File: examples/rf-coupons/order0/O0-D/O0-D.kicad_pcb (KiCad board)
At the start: 4 copper layers, 60.5 x 67.1 mm, 25 parts, among them X17 Anchor, X20 Anchor, X23 Anchor

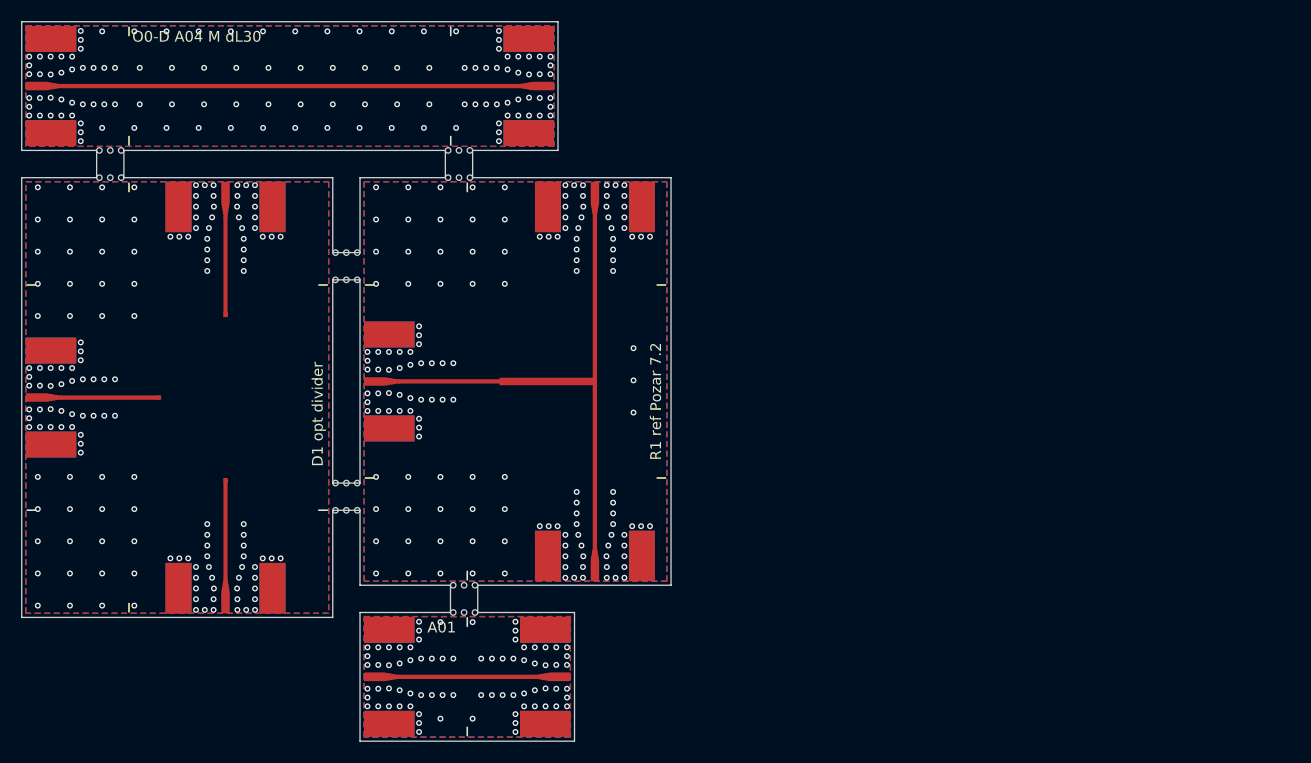
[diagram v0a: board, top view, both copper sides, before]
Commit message: Order 0: the uploads and predictions regenerated after the review
examples/rf-coupons/order0: generated from 73fe6527 (the tag carries it); KiCad
DRC under OSH Park's 4-layer rules 0 violations / 0 unconnected on all three.
`yapnr fab check` (oshpark-4l, oshpark-4l-fr408hr): O0-M 0 errors; O0-W and
O0-D stop on FAB-PLACEHOLDER until D2 and D1 are in (by design); warnings as
before (NPTH in the merged drill file; 1.511 mm of published layers):

- O0-M 120.1 x 144.3 mm, 26.9 sq in, 33 SMAs per copy, 32 tabs;
- O0-W 57.5 x 131.2 mm, 11.7 sq in, 16 SMAs, 15 tabs;
- O0-D 90.6 x 51.5 mm, 7.2 sq in, 12 SMAs, 9 tabs (A20 added).

Every stick has two or more tabs, all on edges without a launch; no plane via
under a silkscreen glyph; no mask web under 0.1 mm; the QR decodes from the
silkscreen render.

Predictions: the coupons on FR408HR and EM528 with the review's roughness
prior, the junction-corrected ring and stub (A12 notch 5.500 GHz FR408HR,
5.388 GHz EM528; A11 1.924 / 5.793 GHz), scalars.json and lines.csv. Boards A
and B regenerated (mask-opening anchors only; DRC unchanged).

docs/rf/order0: sizes and costs, R1/R1t as drawn, the renormalization to the
solver's port impedance (review H3), the C-pad method (M3), the loss basis
(M4), the scalars (L1), the sha256 rule (F9), the connector-fit pre-check, the
mask web note (L2), and the D1/D2 pages with the board around each window.

Co-Authored-By: Claude Opus 5.5 <noreply@anthropic.com>
Claude-Session: https://claude.ai/code/session_01NY8rMuBH8hTFjkoZyuqNZ7
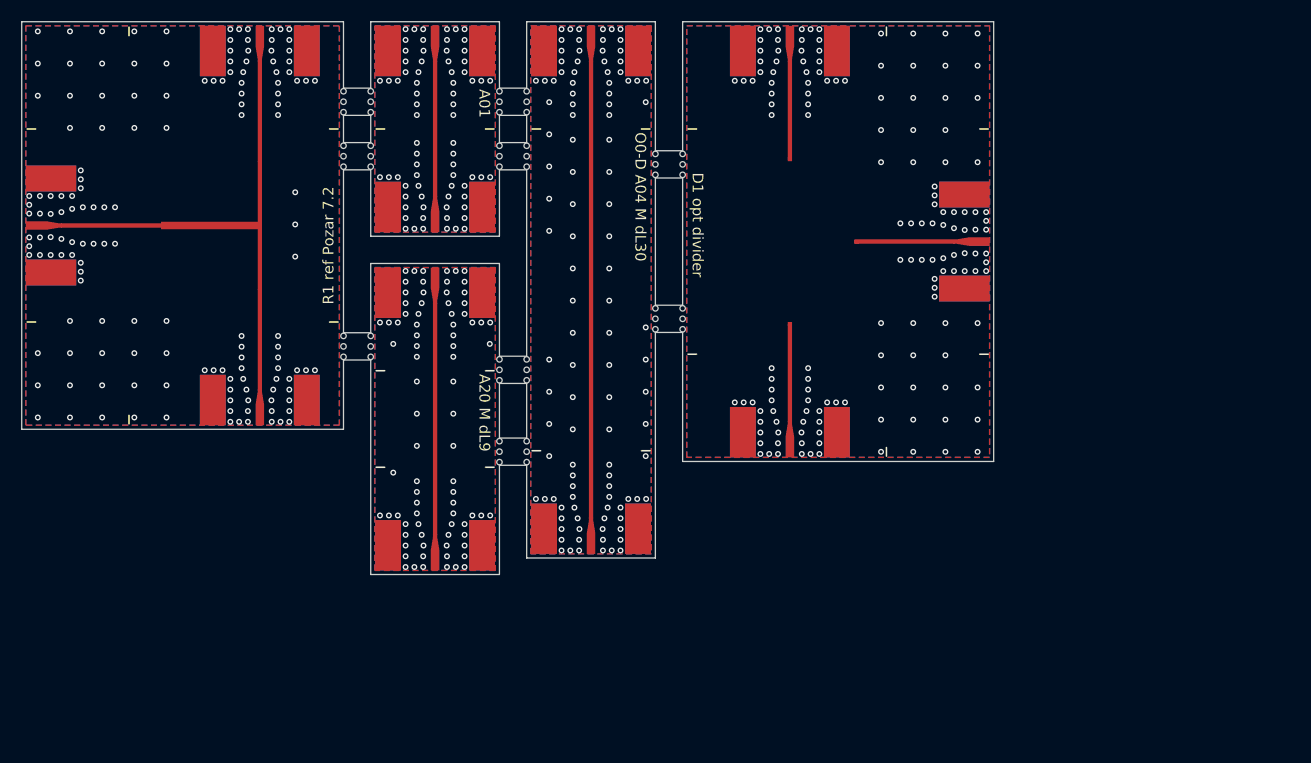
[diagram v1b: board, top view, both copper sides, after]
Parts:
- added JA20E: SMA_EdgeLaunch_Cinch_142-0701-851, SMA_EdgeLaunch_Cinch_142-0701-851, F.Cu at (58.5, 71.5)
- added JA20W: SMA_EdgeLaunch_Cinch_142-0701-851, SMA_EdgeLaunch_Cinch_142-0701-851, F.Cu at (58.5, 42.5)
- added MO_A20: MaskOpening, MaskOpening, F.Cu at (57.3, 45.0)
- added PHD1: Placeholder_D1, Placeholder_D1, F.Cu at (91.6, 40.5)
- moved JD1_1 91.8 mm to (110.6, 40.5), turned to 180 degrees
- moved JD1_3 76.5 mm to (91.6, 20.0), turned to -90 degrees
- moved MO_D1_1 75.0 mm to (97.6, 39.3)
- moved MO_D1_3 70.9 mm to (90.4, 22.5)
- moved X20 66.6 mm to (97.8, 40.5), turned to 180 degrees
- moved JA01W 61.5 mm to (58.5, 20.0), turned to -90 degrees
- moved X26 60.5 mm to (91.6, 32.8), turned to -90 degrees
- moved JD1_2 58.9 mm to (91.6, 61.0), turned to 90 degrees
- moved MO_A01 58.7 mm to (57.3, 22.5)
- moved JA04W 53.4 mm to (73.1, 20.0), turned to -90 degrees
- moved X23 52.6 mm to (91.6, 48.2), turned to 90 degrees
- moved MO_D1_2 52.2 mm to (90.4, 48.0)
- moved MO_D1_W 51.1 mm to (84.6, 32.0)
- moved JA04E 44.1 mm to (73.1, 70.0), turned to 90 degrees
- moved JA01E 43.1 mm to (58.5, 40.0), turned to 90 degrees
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- renumbered X17 to X20, X20 to X23, X23 to X26
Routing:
- net RF_A20: track 0.00 -> 21.6 mm
- net GND_R1: vias 151 -> 149
- net GND_D1: vias 148 -> 146
- net GND_A20: vias 0 -> 81
- net GND_A04: vias 116 -> 107
- net GND_A01: vias 76 -> 72
- added copper zone on B.Cu, net GND_A20
- added copper zone on F.Cu, net GND_A20
- added copper zone on In1.Cu, net GND_A20
- added copper zone on In2.Cu, net GND_A20
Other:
- board size 60.5 x 67.1 mm -> 90.6 x 51.5 mm
- board text added: "A20 M dL9"
- board text added: "O0-D A01"
- board text added: "O0-D A04"
- board text added: "O0-D A20"
- board text added: "O0-D D1"
- board text added: "O0-D R1"
- board text removed: "A04"
- board text removed: "D1"
- board text removed: "R1"

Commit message: Order 0: O0-D regenerated with the re-optimized D1 (part 5/5)
O0-D rebuilt with d1-star re-optimized under PR #53's fixed corner-gap DRC
(docs/rf/order0/predictions/D1-d1c/, label 7e070ca8, supersedes part 2's
ad20e643): KiCad DRC 0 violations, 0 unconnected (headless kicad-cli 10.0.6,
zones refilled); `yapnr fab build` 0 errors (2 pre-existing informational
warnings, same pattern as O0-W's build). Panel grows to 118.2 x 50.0 mm,
9.157 sq in, with its own QR label stick A15 to predictions/D1-d1c.

Gerber zip sha256 pinned in docs/rf/order0/fab/O0-D.sha256 (built at
generator commit 9576c43; zip kept outside this repo in the Splanc
workspace, part5/fab-D/). sha256-manifest.txt regenerated over the whole
docs/rf/order0 tree. README and preregistration.md updated: O0-D's size/
cost, D1's new label and DRC-clean status, and all three solvers' D1
predictions (yapnr.rf: pass, -20.77 dB finer; openEMS: miss, 2.6-3.1 dB
over spec; Palace: not run this round, open item).

tests/unit/rf_coupons/test_order0.py: D1's winner now passes fab DRC
(was a known miss pending this re-optimization); docs/rf/order0/BUILD.bazel's
`winners` filegroup extended to the new D1-d1c winner path so the Bazel data
closure actually contains it.

Co-Authored-By: Claude Opus 5.5 <noreply@anthropic.com>
Claude-Session: https://claude.ai/code/session_01XmUgXgxLjzBpn2W6JpqE2p
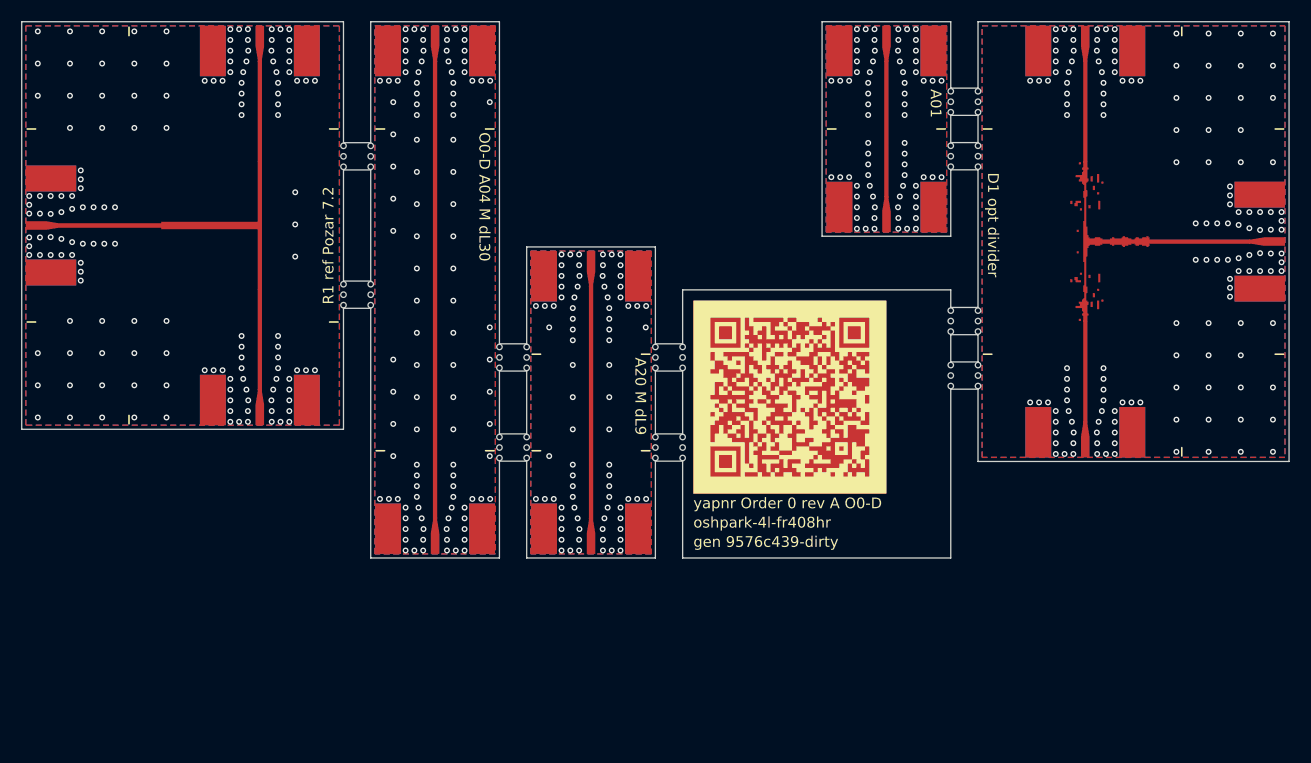
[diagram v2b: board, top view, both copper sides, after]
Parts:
- removed PHD1: Placeholder_D1, Placeholder_D1
- removed X20, X23, X26: Anchor, Anchor
- added UD1: Optimized_D1, Optimized_D1, F.Cu at (119.2, 40.5)
- moved JA01E 42.1 mm to (100.6, 40.0)
- moved JA01W 42.1 mm to (100.6, 20.0)
- moved MO_A01 42.1 mm to (99.4, 22.5)
- moved JD1_1 27.5 mm to (138.2, 40.5)
- moved JD1_2 27.5 mm to (119.2, 61.0)
- moved JD1_3 27.5 mm to (119.2, 20.0)
- moved MO_D1_1 27.5 mm to (125.2, 39.3)
- moved MO_D1_2 27.5 mm to (118.0, 48.0)
- moved MO_D1_3 27.5 mm to (118.0, 22.5)
- moved MO_D1_W 27.5 mm to (112.2, 32.0)
- moved JA20E 14.6 mm to (73.1, 70.0)
- moved JA20W 14.6 mm to (73.1, 41.0)
- moved MO_A20 14.6 mm to (71.9, 43.5)
- moved JA04E 14.5 mm to (58.5, 70.0)
- moved JA04W 14.5 mm to (58.5, 20.0)
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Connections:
- JD1_1 pad 1: RF_D1_1 -> RF_D1
- JD1_2 pad 1: RF_D1_2 -> RF_D1
- JD1_3 pad 1: RF_D1_3 -> RF_D1
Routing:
- net RF_D1: track 0.00 -> 27.9 mm
- net RF_D1_1: track 9.10 -> 0.00 mm
- net RF_D1_3: track 9.09 -> 0.00 mm
- net RF_D1_2: track 9.09 -> 0.00 mm
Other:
- board size 90.6 x 51.5 mm -> 118.2 x 50 mm
- board text added: "7e070ca8"
- board text added: "O0-D A15"
- board text added: "gen 9576c439-dirty"
- board text added: "oshpark-4l-fr408hr"
- board text added: "yapnr Order 0 rev A O0-D"
- board text removed: "D1 window 12 x 15"

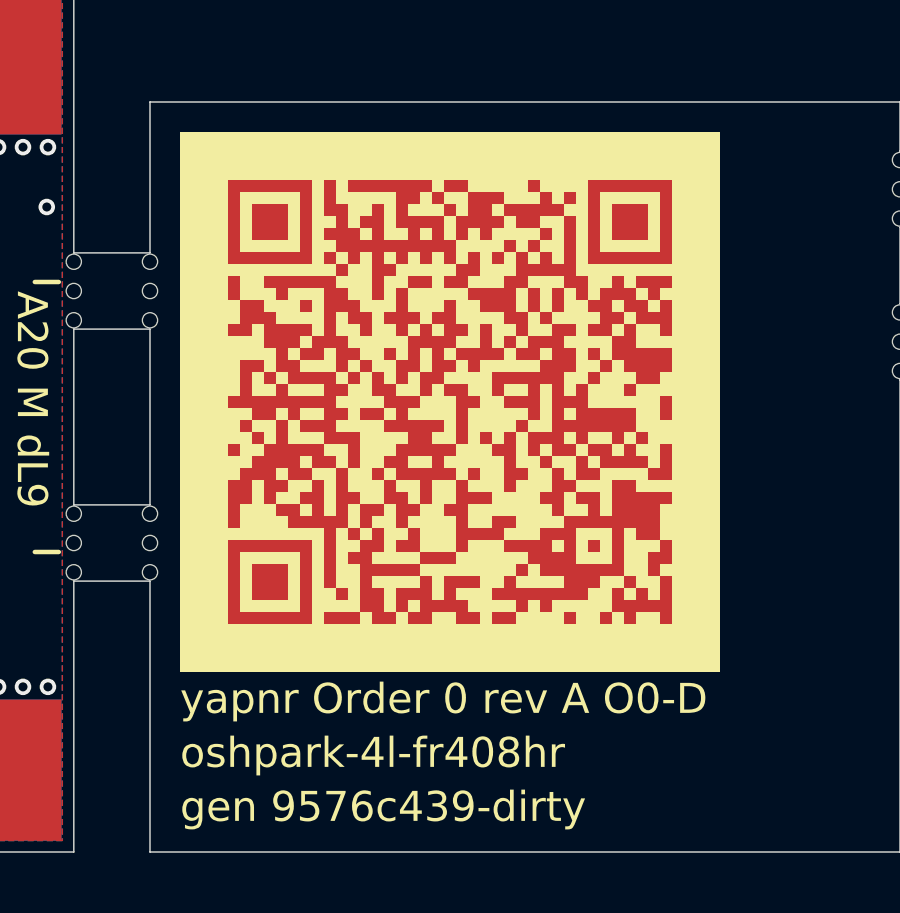
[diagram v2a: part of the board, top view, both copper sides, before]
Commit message: Order 0: O0-D review fixes (clean gen hash, QR to D1-d1c, like-for-like solver text)
- O0-D regenerated at generator commit 0168f32: the silkscreen said
  "gen 9576c439-dirty" while fab/O0-D.sha256 claimed a clean "gen 9576c439";
  the QR stick A15 now decodes to predictions/D1-d1c (was part 2's superseded
  predictions/D1). D1 copper unchanged: board and Gerber F.Cu equal the
  validated footprint (polygon symmetric difference 0). KiCad DRC 0/0,
  fab build 0 errors; new pinned Gerber zip sha256 4c2f8d65...
- images/O0-D.png replotted from the shipped board (it still showed the
  empty placeholder window that its caption no longer described).
- Solver comparison made like for like (openEMS on nominal FR408HR vs
  yapnr.rf M-nom, not M-eq) in README, preregistration and D1-d1c: openEMS
  misses -20 dB |S11| by 2.9 dB; yapnr.rf on M-nom is at the spec line
  (-19.70/-20.02/-20.05 dB), not a clean pass; |dS21| <= 0.14 dB. "All three
  solvers' predictions are registered" corrected (Palace was not run).
- d1-robust: its coarse result [S] (|S11| -0.19 dB, export DRC fails) shows
  the selection could not depend on its timeout.
- Superseded notices on predictions/D1 and the part-2 openEMS D1 rows.
- sha256-manifest.txt refreshed (BUILD.bazel and README.md were stale).

Co-Authored-By: Claude Opus 5.5 <noreply@anthropic.com>
Claude-Session: https://claude.ai/code/session_01XmUgXgxLjzBpn2W6JpqE2p
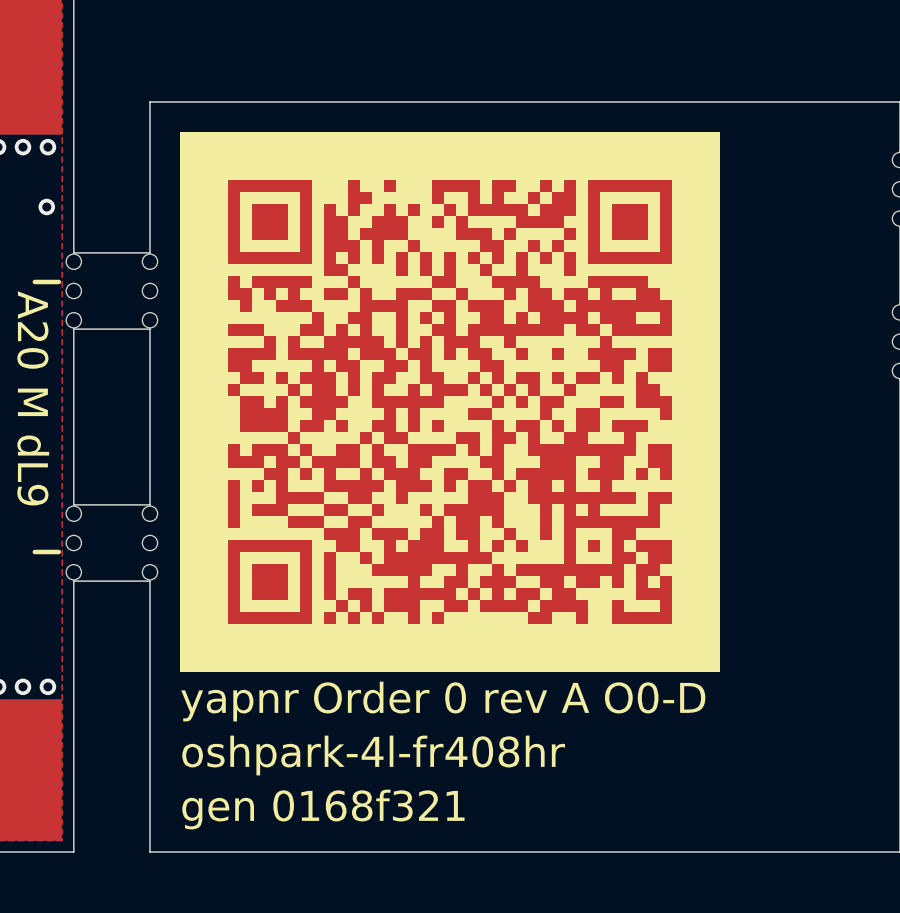
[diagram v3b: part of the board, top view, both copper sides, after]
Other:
- board text added: "gen 0168f321"
- board text removed: "gen 9576c439-dirty"
